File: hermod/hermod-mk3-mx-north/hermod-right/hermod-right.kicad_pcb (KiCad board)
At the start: 2 copper layers, 198.5 x 175.4 mm, 221 parts, among them J1 USB_C_Receptacle_USB2.0, J2 Conn_01x05, J3 USB_C_Receptacle_USB2.0, Q3 MMUN2133LT1G, U1 STM32G474CETx, U2 PRTR5V0U2X, U3 XC6206PxxxMR-Regulator_Linear, U4 CR2013-MI2120, U5 PRTR5V0U2X, U8 SN74AHCT1G125DBVR

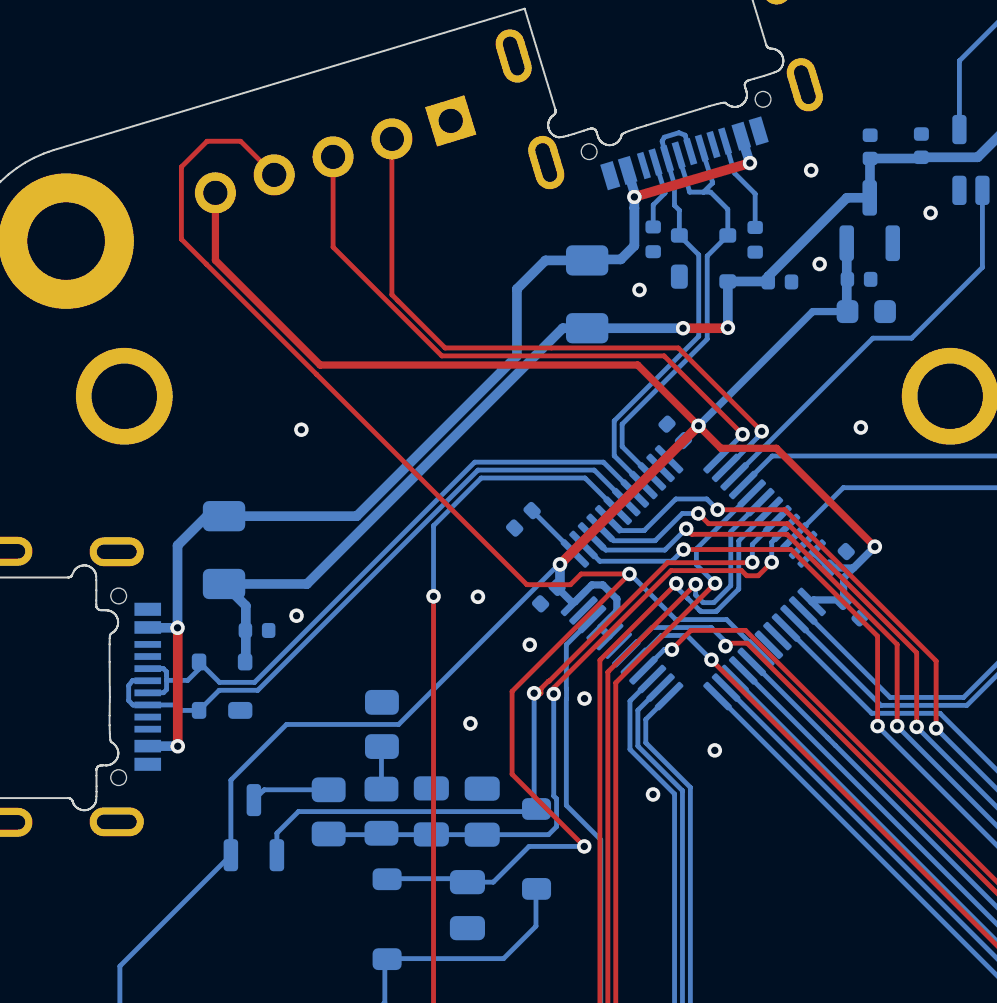
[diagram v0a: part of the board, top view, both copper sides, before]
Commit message: Switched to SRV05-4
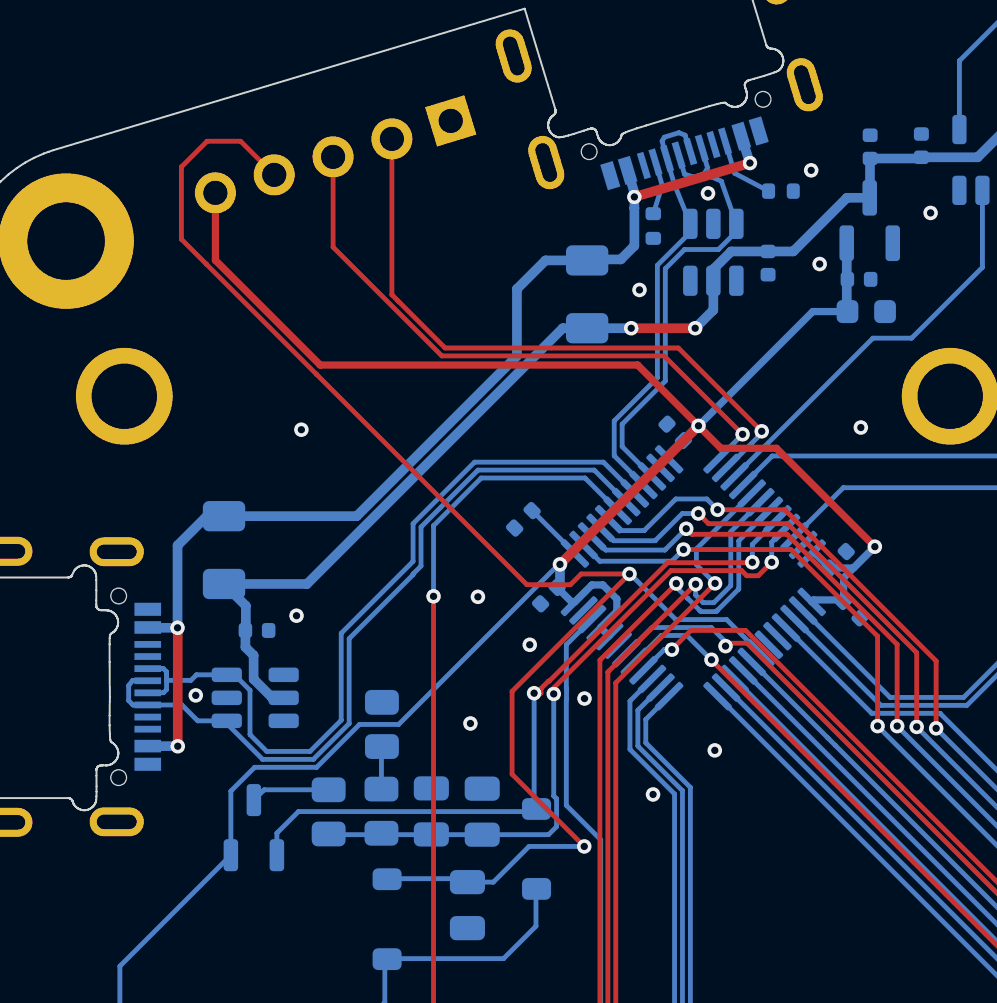
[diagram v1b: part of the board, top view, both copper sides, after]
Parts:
- removed U5: PRTR5V0U2X, Package_TO_SOT_SMD:SOT-143
- added U9: SRV05-4, PCM_marbastlib-various:SOT-23-6-routable, B.Cu at (336.4, 48.4)
- U2: value PRTR5V0U2X -> SRV05-4; footprint Package_TO_SOT_SMD:SOT-143 -> PCM_marbastlib-various:SOT-23-6-routable
- moved U2 25.9 mm to (317.5, 66.8)
- moved R2 2.27 mm to (339.2, 45.8), turned to 0 degrees
- moved C110 0.92 mm to (338.7, 48.8), turned to -90 degrees
- moved R1 0.55 mm to (334.0, 47.3)
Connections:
- U2 pad 1: GND -> SplitSerial-TX
- U2 pad 2: D- -> GND
- U2 pad 3: D+ -> SplitSerial-RX
- U2 pad 4: +5V -> unconnected-(U2-IO3-Pad4)
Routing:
- net SplitSerial-RX: track 26.9 -> 33.1 mm
- net SplitSerial-TX: track 26.9 -> 31.6 mm
- net +5V: track 1242.4 -> 1245.0 mm
- net Net-(J1-CC2): track 3.97 -> 2.97 mm
- net Net-(J1-CC1): track 2.94 -> 2.23 mm
- net GND: vias 65 -> 67
